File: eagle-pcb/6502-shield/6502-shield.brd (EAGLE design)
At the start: 101.6 x 53.3 mm, 65 parts, among them U1 TCB0108-LVL-XLTRTSSOP20, U2 TCB0108-LVL-XLTRTSSOP20, U3 TCB0108-LVL-XLTRTSSOP20, U4 TCB0108-LVL-XLTRTSSOP20, U5 TCB0108-LVL-XLTRTSSOP20, U6 TCB0108-LVL-XLTRTSSOP20

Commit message: more routing work on the pcb but not quite there yet.
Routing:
- net A4: track 19.1 -> 96.3 mm, vias 0 -> 5
- net A6: track 15.2 -> 91.7 mm, vias 0 -> 5
- net A3: track 19.6 -> 93.7 mm, vias 0 -> 5
- net A7: track 14.8 -> 88.0 mm, vias 0 -> 5
- net A8: track 7.98 -> 77.8 mm, vias 0 -> 5
- net A5: track 18.8 -> 87.9 mm, vias 0 -> 5
- net A12: track 9.40 -> 76.9 mm, vias 0 -> 5
- net A10: track 9.77 -> 76.8 mm, vias 0 -> 5
- net A9: track 8.49 -> 75.5 mm, vias 0 -> 5
- net A11: track 10.5 -> 74.6 mm, vias 0 -> 5
- net A14: track 11.5 -> 74.3 mm, vias 0 -> 5
- net A13: track 9.98 -> 71.3 mm, vias 0 -> 5
- net A2: track 19.7 -> 72.0 mm, vias 0 -> 5
- net A0: track 20.1 -> 70.0 mm, vias 0 -> 1
- net A15: track 12.0 -> 58.8 mm, vias 0 -> 1
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
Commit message: Board is routed w/ no erc or drc errors.
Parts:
- added U$1: OSHW_LOGO, 6502-shield:OSHW_LOGO
- moved C21 0.32 mm to (30.8, 25.1)
- moved C3 0.30 mm to (10.4, 34.9)
- moved C18 0.20 mm to (23.7, 18.8)
- moved C10 0.15 mm to (77.0, 42.6)
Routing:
- net D7: track 13.3 -> 118.7 mm, vias 0 -> 6
- net D6: track 14.4 -> 115.9 mm, vias 0 -> 6
- net D5: track 15.6 -> 110.3 mm, vias 0 -> 5
- net D4: track 16.7 -> 109.0 mm, vias 0 -> 5
- net D1: track 13.8 -> 101.1 mm, vias 0 -> 5
- net D3: track 18.1 -> 99.5 mm, vias 0 -> 5
- net D0: track 15.3 -> 95.3 mm, vias 0 -> 5
- net D2: track 19.0 -> 96.6 mm, vias 0 -> 5
- net CLK: track 38.3 -> 102.3 mm, vias 2 -> 4
- net WE: track 23.9 -> 70.6 mm, vias 0 -> 2
- net A1: track 66.1 -> 108.8 mm, vias 1 -> 8
- net A3: track 93.7 -> 131.8 mm, vias 5 -> 8
- net A2: track 72.0 -> 108.0 mm, vias 5 -> 8
- net A0: track 70.0 -> 98.9 mm, vias 1 -> 4
- net A10: track 76.8 -> 103.9 mm, vias 5 -> 6
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- added copper zone on layer 1, net GND
- added copper zone on layer 16, net GND
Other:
- board text added: "5 VDC"
- board text added: "6502-shield REV B"
- board text added: "PA0"
- board text added: "PB0"
- board text removed: "6502-shield REV A"
- board text removed: "PA7"
- board text removed: "PB7"

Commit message: Made some tweaks and random clean up.  Updating the images and a system block diagram.
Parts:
- U$1: device 6502-shield:OSHW_LOGO -> 6502-shield:OSHW_LOGO@1
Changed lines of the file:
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@@
 <layer number="14" name="Route14" color="22" fill="1" visible="no" active="no"/>
 <layer number="15" name="Route15" color="23" fill="1" visible="no" active="no"/>
-<layer number="16" name="Bottom" color="1" fill="1" visible="no" active="yes"/>
+<layer number="16" name="Bottom" color="1" fill="1" visible="yes" active="yes"/>
 <layer number="17" name="Pads" color="2" fill="1" visible="yes" active="yes"/>
 <layer number="18" name="Vias" color="2" fill="1" visible="yes" active="yes"/>
@@
 <layer number="20" name="Dimension" color="24" fill="1" visible="yes" active="yes"/>
 <layer number="21" name="tPlace" color="7" fill="1" visible="yes" active="yes"/>
-<layer number="22" name="bPlace" color="7" fill="1" visible="no" active="yes"/>
+<layer number="22" name="bPlace" color="7" fill="1" visible="yes" active="yes"/>
 <layer number="23" name="tOrigins" color="15" fill="1" visible="yes" active="yes"/>
-<layer number="24" name="bOrigins" color="15" fill="1" visible="no" active="yes"/>
+<layer number="24" name="bOrigins" color="15" fill="1" visible="yes" active="yes"/>
 <layer number="25" name="tNames" color="7" fill="1" visible="yes" active="yes"/>
-<layer number="26" name="bNames" color="7" fill="1" visible="no" active="yes"/>
+<layer number="26" name="bNames" color="7" fill="1" visible="yes" active="yes"/>
 <layer number="27" name="tValues" color="7" fill="1" visible="no" active="yes"/>
 <layer number="28" name="bValues" color="7" fill="1" visible="no" active="yes"/>
@@
 <layer number="38" name="bTest" color="7" fill="1" visible="no" active="yes"/>
 <layer number="39" name="tKeepout" color="4" fill="11" visible="yes" active="yes"/>
-<layer number="40" name="bKeepout" color="1" fill="11" visible="no" active="yes"/>
+<layer number="40" name="bKeepout" color="1" fill="11" visible="yes" active="yes"/>
 <layer number="41" name="tRestrict" color="4" fill="10" visible="yes" active="yes"/>
-<layer number="42" name="bRestrict" color="1" fill="10" visible="no" active="yes"/>
+<layer number="42" name="bRestrict" color="1" fill="10" visible="yes" active="yes"/>
 <layer number="43" name="vRestrict" color="2" fill="10" visible="no" active="yes"/>
 <layer number="44" name="Drills" color="7" fill="1" visible="no" active="yes"/>
@@
 <layer number="50" name="dxf" color="7" fill="1" visible="no" active="no"/>
 <layer number="51" name="tDocu" color="7" fill="1" visible="yes" active="yes"/>
-<layer number="52" name="bDocu" color="7" fill="1" visible="no" active="yes"/>
+<layer number="52" name="bDocu" color="7" fill="1" visible="yes" active="yes"/>
 <layer number="53" name="tGND_GNDA" color="7" fill="9" visible="no" active="no"/>
 <layer number="54" name="bGND_GNDA" color="1" fill="9" visible="no" active="no"/>
@@
 <attribute name="VALUE" x="2.75" y="50.2501" size="0.02" layer="27" rot="R270"/>
 </element>
-<element name="EXT_XO" library="6502-shield" library_urn="urn:adsk.eagle:library:18477216" package="DIP8/4" package3d_urn="urn:adsk.eagle:package:18885296/3" value="CRYSTAL-OSC-DIP8/4" x="8.9" y="41" smashed="yes" rot="R270">
+<element name="EXT_XO" library="6502-shield" library_urn="urn:adsk.eagle:library:18477216" package="DIP8/4" package3d_urn="urn:adsk.eagle:package:18885296/4" value="CRYSTAL-OSC-DIP8/4" x="8.9" y="41" smashed="yes" rot="R270">
 <attribute name="VALUE" x="2.9" y="45" size="1.27" layer="27" rot="R270"/>
 </element>
@@
 <attribute name="VALUE" x="46.94" y="43.83" size="1.27" layer="27" rot="R90"/>
 </element>
-<element name="U$1" library="6502-shield" library_urn="urn:adsk.eagle:library:18477216" package="OSHW_LOGO" value="OSHW_LOGO" x="72" y="15.5" smashed="yes"/>
+<element name="U$1" library="6502-shield" library_urn="urn:adsk.eagle:library:18477216" package="OSHW_LOGO@1" value="OSHW_LOGO" x="72" y="15.5" smashed="yes"/>
 </elements>
 <signals>
@@
 </signal>
 <signal name="OE">
-<contactref element="RAM" pad="1"/>
 <contactref element="EEPROM" pad="1"/>
 <contactref element="FPGA" pad="66"/>
@@
 <wire x1="74" y1="43.5" x2="74" y2="44" width="0.1524" layer="1"/>
 <wire x1="47" y1="40.1952" x2="47.575" y2="40.7702" width="0.1524" layer="1"/>
-<wire x1="47.575" y1="40.7702" x2="47.575" y2="41.9394" width="0.1524" layer="1"/>
 <wire x1="62.91404375" y1="41.9394" x2="62.91404375" y2="40.48115625" width="0.1524" layer="1"/>
 <wire x1="62.91404375" y1="40.48115625" x2="63.2" y2="40.1952" width="0.1524" layer="1"/>
+<contactref element="RAM" pad="1"/>
+<wire x1="47.575" y1="40.7702" x2="47.575" y2="41.9394" width="0.1524" layer="1"/>
 </signal>
 <signal name="WE">

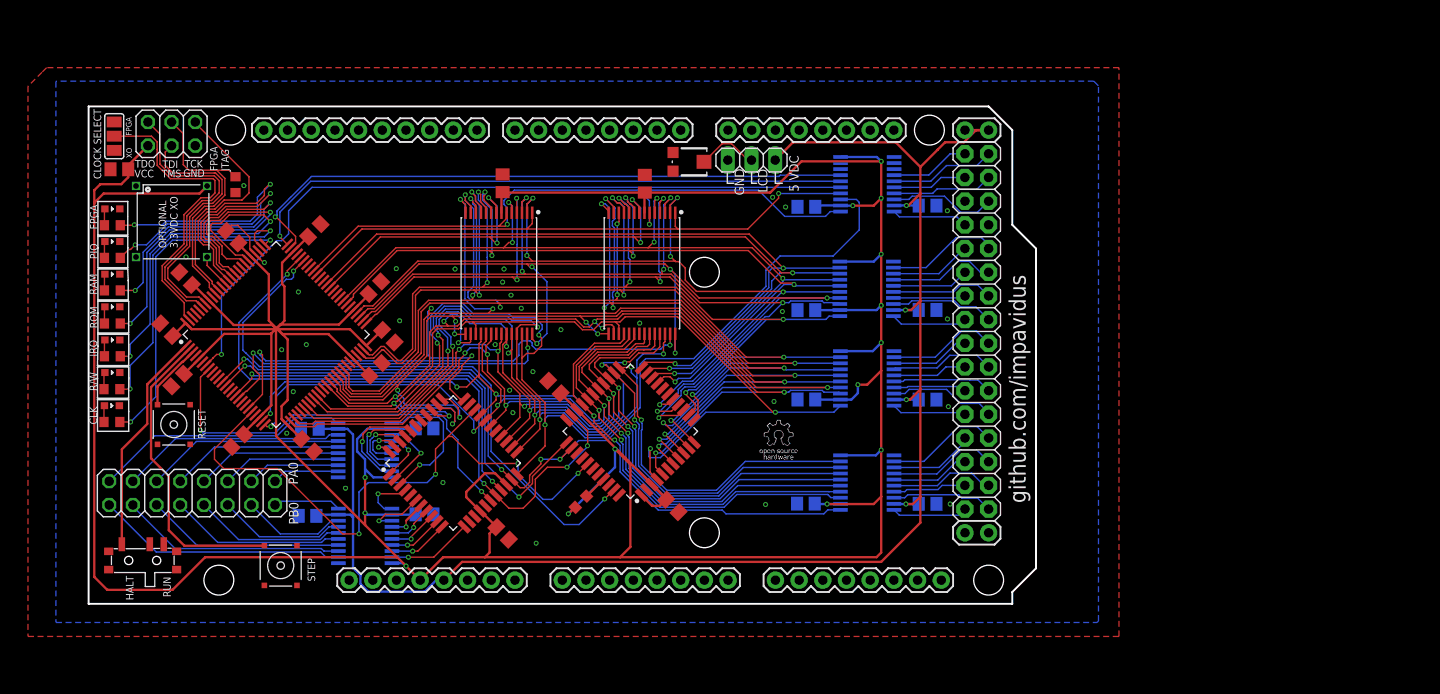
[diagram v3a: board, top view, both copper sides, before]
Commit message: fixed. verified footprint with the printer. still need to generate new camoutputs, etc.
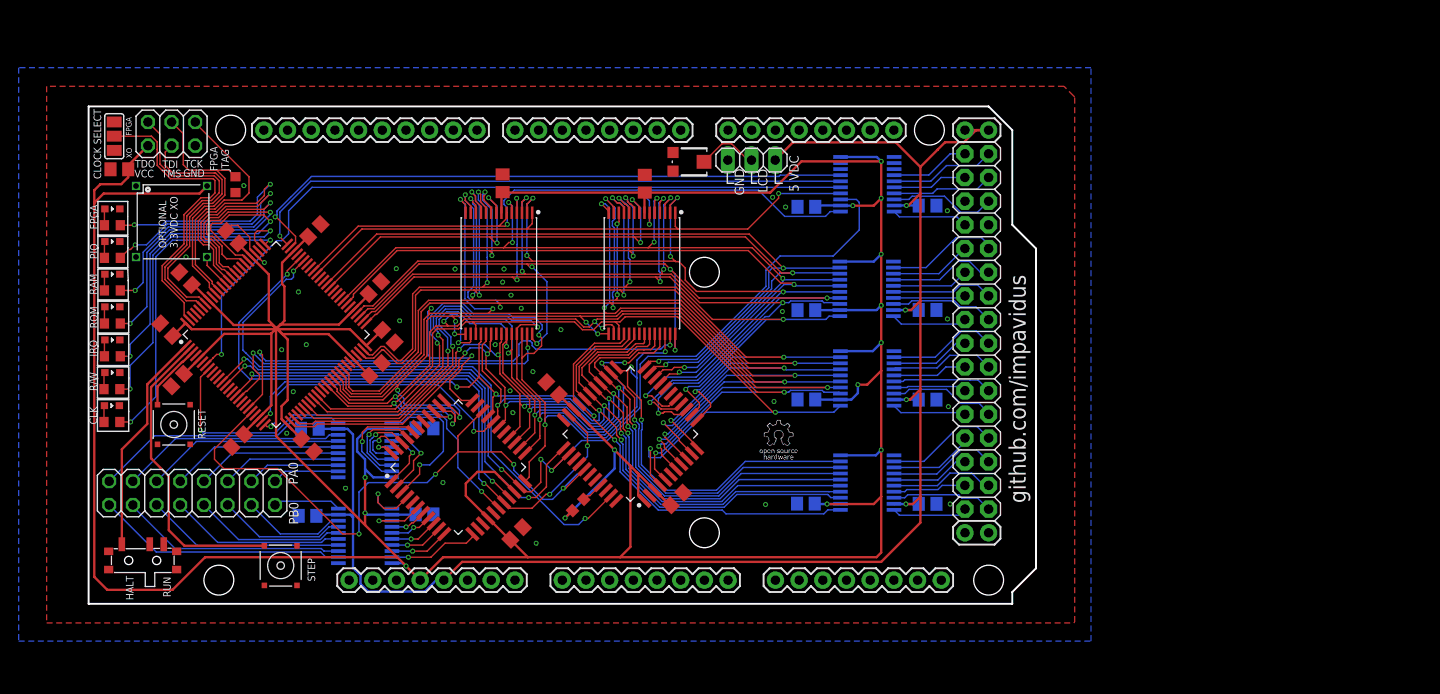
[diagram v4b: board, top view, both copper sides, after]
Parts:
- CPU, PIO: device 6502-shield:QFP80P1200X1200X160-44N -> 6502-shield:QFP80P1320X1320X270-44N
- moved C24 1.50 mm to (45.9, 7.55), turned to 45 degrees
- moved C26 0.90 mm to (63.1, 11.2), turned to 45 degrees
- moved PIO 0.71 mm to (39.6, 14.7)
- moved R18 0.46 mm to (52.5, 10.6)
- moved CPU 0.30 mm to (58.1, 18.2)
- moved C25 0.25 mm to (49.8, 23.1)
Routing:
- net A11: track 94.6 -> 98.0 mm
- net CLK: track 102.3 -> 105.2 mm
- net RESETN: track 67.8 -> 69.9 mm
- net PB0: track 5.77 -> 7.52 mm
- net A3: track 131.8 -> 133.5 mm
- net VCC: track 524.1 -> 525.7 mm
- net IRQ_IO: track 45.2 -> 46.3 mm
- net IO_EN: track 40.0 -> 41.2 mm
- net PA5: track 5.63 -> 6.76 mm
- net A7: track 102.7 -> 103.6 mm
- net A10: track 103.9 -> 104.8 mm
- net A9: track 97.1 -> 98.0 mm
- net PA3: track 5.68 -> 6.48 mm
- net A12: track 96.4 -> 95.7 mm
- net A4: track 117.9 -> 118.6 mm
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
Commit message: Overlooked that tactile switch pads were very small for hand soldering so enlarged them.  Created new models, gerbers, and images.
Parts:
- PB_RESET, PB_STEP: device 6502-shield:MCSLPT4644B1TR-TACT-SW -> 6502-shield:MCSLPT4644B1TR-TACT-SW-NEW
- moved PB_STEP 2.97 mm to (22.7, 6.20)
- moved PB_RESET 2.87 mm to (11.1, 21.3)
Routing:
- net PB_STEP: track 32.9 -> 31.4 mm
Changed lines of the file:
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@@
 <text x="8" y="2.9" size="0.8128" layer="21" font="vector" ratio="15" rot="R270">RUN</text>
 <text x="4" y="3" size="0.8128" layer="21" font="vector" ratio="15" rot="R270">HALT</text>
-<text x="24.3" y="2.4" size="0.8128" layer="21" font="vector" ratio="15" rot="R90">STEP</text>
+<text x="24.25" y="2.75" size="0.8128" layer="21" font="vector" ratio="15" rot="R90">STEP</text>
 <text x="12.55" y="17.65" size="0.8128" layer="21" font="vector" ratio="15" rot="R90">RESET</text>
 <text x="1.35" y="45.55" size="0.8128" layer="21" font="vector" ratio="15" rot="R90">CLOCK SELECT</text>
@@
 <elements>
 <element name="PCB1" library="E14_Arduino_revC" library_urn="urn:adsk.eagle:library:18477430" package="ARDUINO_MEGA2560" package3d_urn="urn:adsk.eagle:package:18477461/7" value="ARDUINO_MEGA2560" x="0" y="0" locked="yes" smashed="yes"/>
-<element name="PB_RESET" library="6502-shield" library_urn="urn:adsk.eagle:library:18477216" package="MCSLPT4644B1TR-TACT-SW" package3d_urn="urn:adsk.eagle:package:18592201/6" value="MCSLPT4644B1TR-TACT-SW" x="9.14" y="19.23" smashed="yes" rot="R270">
-<attribute name="VALUE" x="5.24" y="22.53" size="1.27" layer="27" rot="R270"/>
+<element name="PB_RESET" library="6502-shield" library_urn="urn:adsk.eagle:library:18477216" package="MCSLPT4644B1TR-TACT-SW-NEW" package3d_urn="urn:adsk.eagle:package:19789458/2" value="MCSLPT4644B1TR-TACT-SW" x="11.09" y="21.33" smashed="yes" rot="R270">
+<attribute name="VALUE" x="7.19" y="24.63" size="1.27" layer="27" rot="R270"/>
 </element>
 <element name="SW_RUNHALT" library="6502-shield" library_urn="urn:adsk.eagle:library:18477216" package="PCM12SMTR" package3d_urn="urn:adsk.eagle:package:18622137/7" value="PCM12SMTR-SPDT-RIGHT-ANG" x="5.8" y="4.65" smashed="yes">
@@
 <attribute name="VALUE" x="63.11529375" y="23.215290625" size="1.27" layer="27" rot="R135" align="top-center"/>
 </element>
-<element name="PB_STEP" library="6502-shield" library_urn="urn:adsk.eagle:library:18477216" package="MCSLPT4644B1TR-TACT-SW" package3d_urn="urn:adsk.eagle:package:18592201/6" value="MCSLPT4644B1TR-TACT-SW" x="20.6" y="4.1" smashed="yes" rot="R270">
-<attribute name="VALUE" x="16.7" y="7.4" size="1.27" layer="27" rot="R270"/>
+<element name="PB_STEP" library="6502-shield" library_urn="urn:adsk.eagle:library:18477216" package="MCSLPT4644B1TR-TACT-SW-NEW" package3d_urn="urn:adsk.eagle:package:19789458/2" value="MCSLPT4644B1TR-TACT-SW" x="22.7" y="6.2" smashed="yes" rot="R270">
+<attribute name="VALUE" x="18.8" y="9.5" size="1.27" layer="27" rot="R270"/>
 </element>
 <element name="R3" library="rcl" library_urn="urn:adsk.eagle:library:334" package="R0603" package3d_urn="urn:adsk.eagle:package:23555/3" value="4.7K" x="15.75" y="44.95" smashed="yes" rot="R90">
@@
 <contactref element="FPGA" pad="1"/>
 <contactref element="SW_RUNHALT" pad="1"/>
-<wire x1="6.2936" y1="23.540790625" x2="10.44251875" y2="27.689709375" width="0.254" layer="1"/>
-<wire x1="3.5648" y1="6.3899" x2="3.5648" y2="16.5648" width="0.254" layer="1"/>
-<wire x1="3.5648" y1="16.5648" x2="6.2936" y2="19.2936" width="0.254" layer="1"/>
-<wire x1="6.2936" y1="19.2936" x2="6.2936" y2="23.540790625" width="0.254" layer="1"/>
+<wire x1="6.2936" y1="23.540790625" x2="10.44251875" y2="27.689709375" width="0.1524" layer="1"/>
+<wire x1="3.5648" y1="6.3899" x2="3.5648" y2="16.5648" width="0.1524" layer="1"/>
+<wire x1="3.5648" y1="16.5648" x2="6.2936" y2="19.2936" width="0.1524" layer="1"/>
+<wire x1="6.2936" y1="19.2936" x2="6.2936" y2="23.540790625" width="0.1524" layer="1"/>
 </signal>
 <signal name="PB_STEP">
 <contactref element="FPGA" pad="2"/>
 <contactref element="PB_STEP" pad="T3"/>
-<wire x1="6.7" y1="23.240084375" x2="10.796071875" y2="27.33615625" width="0.254" layer="1"/>
-<wire x1="18.85" y1="6.225" x2="10.275" y2="6.225" width="0.254" layer="1"/>
-<wire x1="10.275" y1="6.225" x2="8.6" y2="7.9" width="0.254" layer="1"/>
-<wire x1="8.6" y1="7.9" x2="8.6" y2="13.7" width="0.254" layer="1"/>
-<wire x1="8.6" y1="13.7" x2="6.7" y2="15.6" width="0.254" layer="1"/>
-<wire x1="6.7" y1="15.6" x2="6.7" y2="23.240084375" width="0.254" layer="1"/>
+<wire x1="6.7" y1="23.240084375" x2="10.796071875" y2="27.33615625" width="0.1524" layer="1"/>
+<wire x1="19.2" y1="6.2" x2="8.6" y2="9.500365625" width="0.1524" layer="1"/>
+<wire x1="8.6" y1="9.500365625" x2="8.6" y2="13.7" width="0.1524" layer="1"/>
+<wire x1="8.6" y1="13.7" x2="6.7" y2="15.6" width="0.1524" layer="1"/>
+<wire x1="6.7" y1="15.6" x2="6.7" y2="23.240084375" width="0.1524" layer="1"/>
 </signal>
 <signal name="PB_RESET">
 <contactref element="PB_RESET" pad="T3"/>
 <contactref element="FPGA" pad="3"/>
-<wire x1="11.149625" y1="26.982603125" x2="10.108121875" y2="25.9411" width="0.254" layer="1"/>
-<wire x1="10.108121875" y1="25.9411" x2="10.035309375" y2="25.9411" width="0.254" layer="1"/>
-<wire x1="10.035309375" y1="25.9411" x2="7.39" y2="23.295790625" width="0.254" layer="1"/>
-<wire x1="7.39" y1="23.295790625" x2="7.39" y2="21.355" width="0.254" layer="1"/>
+<wire x1="10.449625" y1="26.382603125" x2="7.208121875" y2="23.1411" width="0.1524" layer="1"/>
+<wire x1="7.208121875" y1="23.1411" x2="7.208121875" y2="21.711878125" width="0.1524" layer="1"/>
+<wire x1="7.59" y1="21.33" x2="7.208121875" y2="21.711878125" width="0.1524" layer="1"/>
+<wire x1="11.149625" y1="26.982603125" x2="10.549625" y2="26.382603125" width="0.1524" layer="1"/>
+<wire x1="10.549625" y1="26.382603125" x2="10.449625" y2="26.382603125" width="0.1524" layer="1"/>
 </signal>
 <signal name="TMS">
